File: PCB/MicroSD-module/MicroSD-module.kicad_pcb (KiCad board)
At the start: 2 copper layers, 24.4 x 41.9 mm, 16 parts, among them J1 Connector, K1 HYC77-TF09-200, U1 SE5218, U2 TXB0104PWR

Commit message: More OCD
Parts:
- moved C1 10.3 mm to (127.5, 111.9), turned to -90 degrees
- moved U1 8.39 mm to (130.0, 112.4)
- moved C2 8.13 mm to (132.7, 111.8)
- moved C3 4.46 mm to (124.7, 117.8)
- renumbered C3 to C2, C2 to C3
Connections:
- K1 pad SHIELD: (no net) -> GND
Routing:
- net GND: track 4.53 -> 41.7 mm, vias 7 -> 0
- net 5V_burgerDisk: track 46.5 -> 30.2 mm
- net 3V3: track 25.4 -> 30.6 mm, vias 2 -> 0
- net CS: track 23.9 -> 25.6 mm
- net MOSI_L: track 12.3 -> 14.0 mm
- net MISO: track 27.5 -> 28.5 mm
- net CS_L: track 14.6 -> 15.5 mm
- net MISO_L: track 9.04 -> 9.73 mm
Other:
- board text added: "https://colino.net"
- board text added: "© Colin Leroy-Mira"

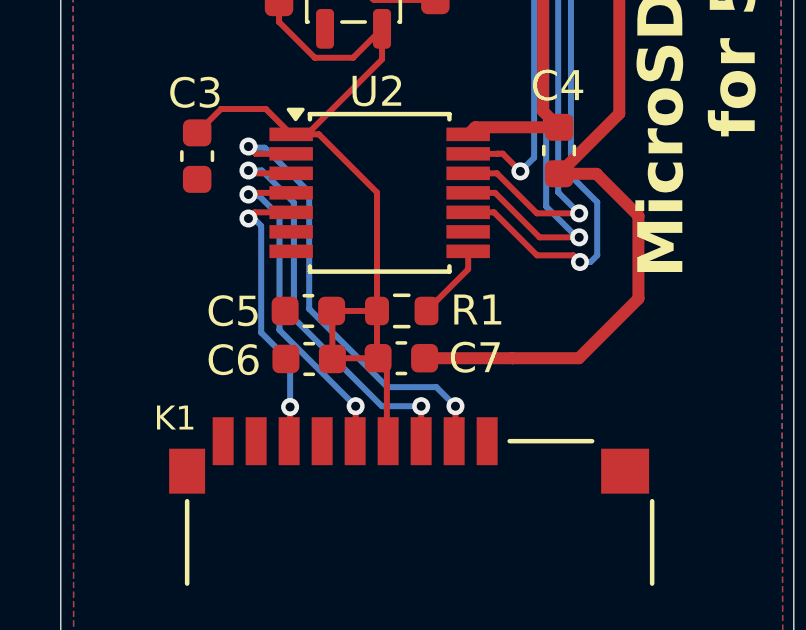
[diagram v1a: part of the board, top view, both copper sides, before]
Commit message: Fix microSD caps
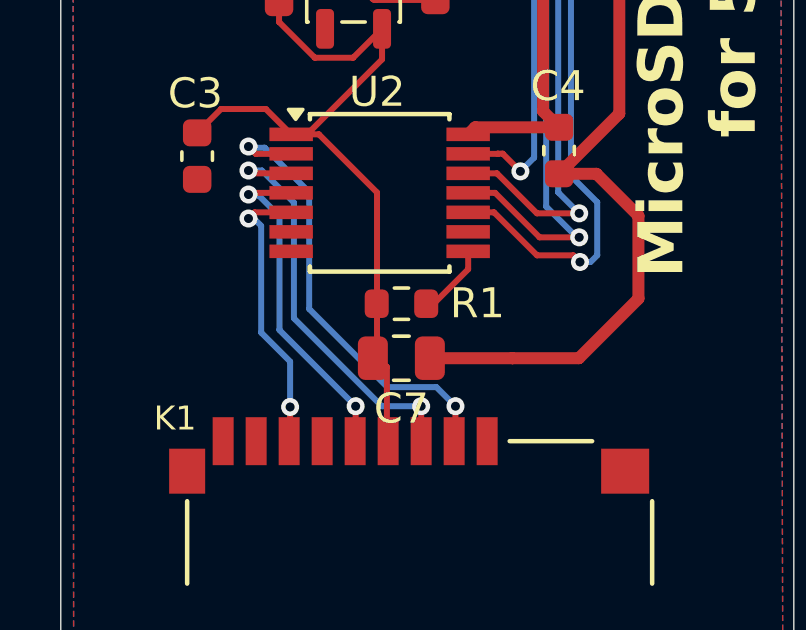
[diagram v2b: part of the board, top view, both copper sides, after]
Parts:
- removed C5: 100n, Capacitor_SMD:C_0603_1608Metric
- removed C6: 2u2, Capacitor_SMD:C_0603_1608Metric
- C7: value 100n -> 22uf; footprint Capacitor_SMD:C_0603_1608Metric -> Capacitor_SMD:C_0805_2012Metric
- moved R1 0.24 mm to (131.6, 122.7)
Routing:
- net 3V3: track 30.6 -> 26.0 mm

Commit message: OCD
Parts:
- moved C4 0.41 mm to (136.4, 117.6)
- renumbered C7 to C5
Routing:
- net 3V3: track 26.0 -> 27.8 mm
- net CS: track 25.6 -> 24.5 mm
- net GND: track 41.7 -> 42.4 mm
- net 5V_burgerDisk: track 30.2 -> 29.6 mm
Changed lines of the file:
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@@
 		(descr "Capacitor SMD 0805 (2012 Metric), square (rectangular) end terminal, IPC_7351 nominal, (Body size source: IPC-SM-782 page 76, https://www.pcb-3d.com/wordpress/wp-content/uploads/ipc-sm-782a_amendment_1_and_2.pdf, https://docs.google.com/spreadsheets/d/1BsfQQcO9C6DZCsRaXUlFlo91Tg2WpOkGARC1WS5S8t0/edit?usp=sharing), generated with kicad-footprint-generator")
 		(tags "capacitor")
-		(property "Reference" "C7"
-			(at 0 -1.68 180)
+		(property "Reference" "C5"
+			(at -2.7634 0.0362 180)
 			(layer "F.SilkS")
 			(effects
@@
 	(footprint "Capacitor_SMD:C_0603_1608Metric"
 		(layer "F.Cu")
-		(at 136.8044 117.6144 90)
+		(at 136.39 117.62 90)
 		(descr "Capacitor SMD 0603 (1608 Metric), square (rectangular) end terminal, IPC-7351 nominal, (Body size source: IPC-SM-782 page 76, https://www.pcb-3d.com/wordpress/wp-content/uploads/ipc-sm-782a_amendment_1_and_2.pdf), generated with kicad-footprint-generator")
 		(tags "capacitor")
@@
 	)
 	(segment
-		(start 138.0494 118.3894)
-		(end 136.8044 118.3894)
-		(width 0.4)
-		(layer "F.Cu")
-		(net 1)
-	)
-	(segment
-		(start 139.45 122.55)
-		(end 139.45 119.79)
+		(start 136.39 118.395)
+		(end 136.7988 118.395)
 		(width 0.4)
 		(layer "F.Cu")
@@
 	)
 	(segment
-		(start 136.8044 118.3894)
-		(end 138.811 116.3828)
+		(start 138.811 116.3828)
+		(end 138.811 100.3046)
 		(width 0.4)
 		(layer "F.Cu")
@@
 	)
 	(segment
-		(start 132.554 112.494)
-		(end 132.68 112.62)
+		(start 139.45 122.55)
+		(end 139.45 119.79)
 		(width 0.4)
 		(layer "F.Cu")
@@
 	)
 	(segment
-		(start 137.4638 124.5362)
-		(end 139.45 122.55)
+		(start 136.7988 118.395)
+		(end 138.811 116.3828)
 		(width 0.4)
 		(layer "F.Cu")
@@
 	)
 	(segment
-		(start 139.45 119.79)
-		(end 138.0494 118.3894)
+		(start 136.3956 118.3894)
+		(end 136.39 118.395)
 		(width 0.4)
 		(layer "F.Cu")
@@
 	)
 	(segment
-		(start 135.2462 124.5362)
-		(end 137.4638 124.5362)
+		(start 138.0494 118.3894)
+		(end 136.3956 118.3894)
 		(width 0.4)
 		(layer "F.Cu")
@@
 	)
 	(segment
-		(start 129.9525 111.2825)
-		(end 129.9525 111.944999)
+		(start 135.2462 124.5362)
+		(end 137.4638 124.5362)
 		(width 0.4)
 		(layer "F.Cu")
@@
 	)
 	(segment
-		(start 138.811 116.3828)
-		(end 138.811 100.3046)
+		(start 129.9525 111.2825)
+		(end 129.9525 111.944999)
 		(width 0.4)
 		(layer "F.Cu")
@@
 	)
 	(segment
+		(start 137.4638 124.5362)
+		(end 139.45 122.55)
+		(width 0.4)
+		(layer "F.Cu")
+		(net 1)
+	)
+	(segment
+		(start 139.45 119.79)
+		(end 138.0494 118.3894)
+		(width 0.4)
+		(layer "F.Cu")
+		(net 1)
+	)
+	(segment
 		(start 135.2462 124.5362)
 		(end 135.25 124.54)
@@
 	)
 	(segment
-		(start 135.514165 118.308035)
+		(start 134.93613 117.73)
 		(end 134.92413 117.718)
 		(width 0.2)
@@
 	)
 	(segment
-		(start 134.75567 117.7244)
-		(end 133.7734 117.7244)
+		(start 134.76207 117.718)
+		(end 134.75567 117.7244)
 		(width 0.2)
 		(layer "F.Cu")
@@
 	)
 	(segment
-		(start 134.76207 117.718)
-		(end 134.75567 117.7244)
+		(start 134.75567 117.7244)
+		(end 133.7734 117.7244)
+		(width 0.2)
+		(layer "F.Cu")
+		(net 2)
+	)
+	(segment
+		(start 135.1 117.73)
+		(end 134.93613 117.73)
 		(width 0.2)
 		(layer "F.Cu")
@@
 	)
 	(via
-		(at 135.514165 118.308035)
+		(at 135.1 117.73)
 		(size 0.6)
 		(drill 0.3)
@@
 	)
 	(segment
-		(start 135.9716 117.8506)
-		(end 135.9716 107.8716)
+		(start 135.9716 107.8716)
+		(end 130.17 102.07)
 		(width 0.2)
 		(layer "B.Cu")
@@
 	)
 	(segment
-		(start 135.9716 107.8716)
-		(end 130.17 102.07)
+		(start 135.1 117.73)
+		(end 135.9716 116.8584)
 		(width 0.2)
 		(layer "B.Cu")
@@
 	)
 	(segment
-		(start 130.17 102.07)
-		(end 127.8764 102.07)
+		(start 135.9716 116.8584)
+		(end 135.9716 107.8716)
 		(width 0.2)
 		(layer "B.Cu")
@@
 	)
 	(segment
-		(start 135.514165 118.308035)
-		(end 135.9716 117.8506)
+		(start 130.17 102.07)
+		(end 127.8764 102.07)
 		(width 0.2)
 		(layer "B.Cu")
@@
 	)
 	(segment
+		(start 136.39 116.845)
+		(end 136.3844 116.8394)
+		(width 0.4)
+		(layer "F.Cu")
+		(net 6)
+	)
+	(segment
+		(start 136.3844 116.8394)
+		(end 134.0084 116.8394)
+		(width 0.4)
+		(layer "F.Cu")
+		(net 6)
+	)
+	(segment
 		(start 132.68 111.07)
 		(end 134.23 111.07)
@@
 	)
 	(segment
+		(start 136.271 108.5)
+		(end 136.271 116.306)
+		(width 0.4)
+		(layer "F.Cu")
+		(net 6)
+	)
+	(segment
 		(start 130.9025 111.2825)
 		(end 132.4675 111.2825)
@@
 	)
 	(segment
-		(start 136.271 116.306)
-		(end 136.8044 116.8394)
+		(start 130.501499 110.219)
+		(end 130.9025 110.620001)
 		(width 0.4)
 		(layer "F.Cu")
@@
 	)
 	(segment
-		(start 130.501499 110.219)
-		(end 130.9025 110.620001)
+		(start 136.39 116.425)
+		(end 136.39 116.845)
 		(width 0.4)
 		(layer "F.Cu")
@@
 	)
 	(segment
-		(start 129.570112 110.219)
-		(end 130.501499 110.219)
+		(start 136.271 116.306)
+		(end 136.39 116.425)
 		(width 0.4)
 		(layer "F.Cu")
@@
 	)
 	(segment
-		(start 136.271 108.5)
-		(end 136.271 116.306)
+		(start 129.570112 110.219)
+		(end 130.501499 110.219)
 		(width 0.4)
 		(layer "F.Cu")
@@
 	)
 	(segment
-		(start 136.8044 116.8394)
-		(end 134.0084 116.8394)
-		(width 0.4)
+		(start 130.7348 119.0108)
+		(end 130.9025 118.8431)
+		(width 0.2)
 		(layer "F.Cu")
-		(net 6)
+		(net 7)
 	)
 	(segment
@@
 	)
 	(segment
-		(start 127.8734 117.0744)
-		(end 128.7984 117.0744)
-		(width 0.2)
-		(layer "F.Cu")
-		(net 7)
-	)
-	(segment
 		(start 130.7348 119.0108)
 		(end 130.7348 122.7102)
@@
 	)
 	(segment
-		(start 124.74 117.025)
-		(end 125.535 116.23)
+		(start 130.9025 118.8431)
+		(end 130.9025 113.5575)
 		(width 0.2)
 		(layer "F.Cu")
@@
 	)
 	(segment
-		(start 128.7984 117.0744)
-		(end 130.7348 119.0108)
+		(start 124.74 117.025)
+		(end 125.535 116.23)
 		(width 0.2)
 		(layer "F.Cu")

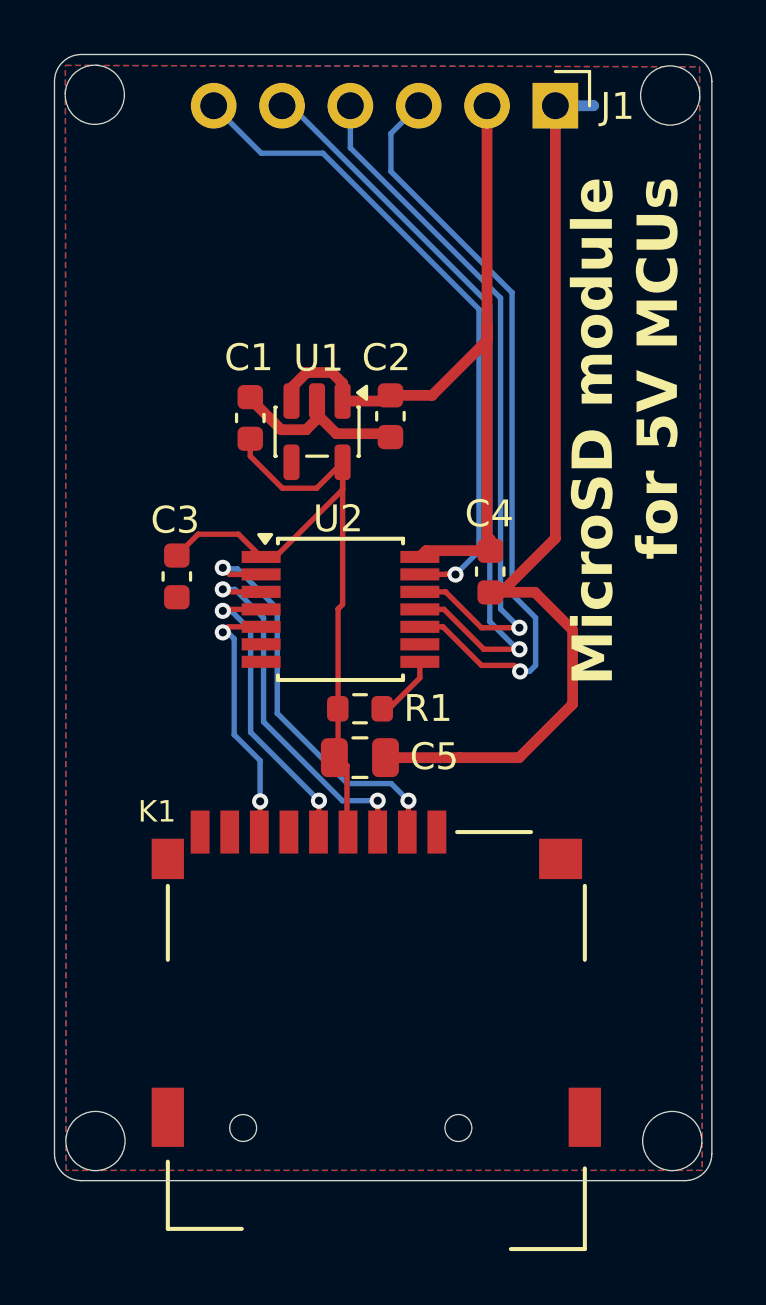
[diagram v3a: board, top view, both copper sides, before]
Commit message: fatter traces
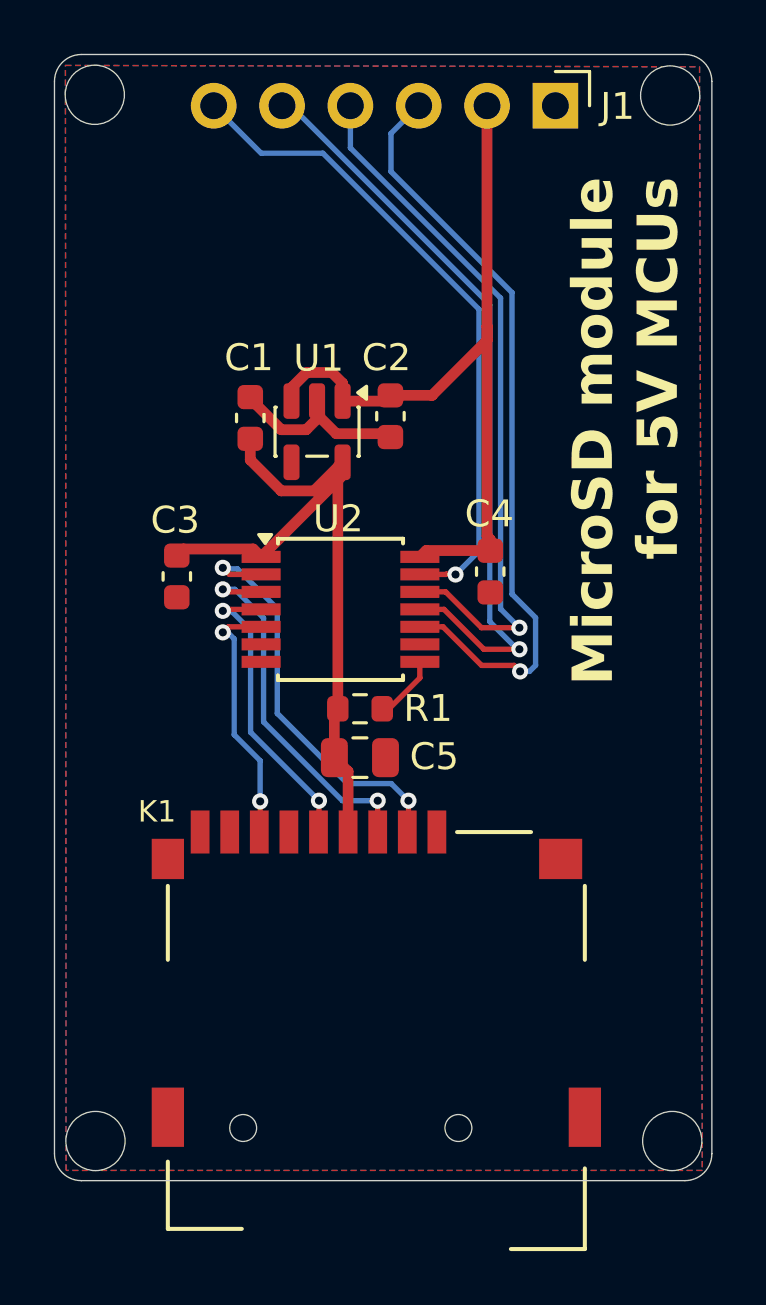
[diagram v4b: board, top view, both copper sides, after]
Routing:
- net GND: track 42.4 -> 7.24 mm
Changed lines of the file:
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@@
-	)
-	(segment
-		(start 136.39 118.395)
-		(end 136.7988 118.395)
-		(width 0.4)
-		(layer "F.Cu")
-		(net 1)
-	)
-	(segment
-		(start 132.3216 124.5362)
-		(end 135.2462 124.5362)
-		(width 0.4)
-		(layer "F.Cu")
-		(net 1)
-	)
-	(segment
-		(start 138.811 116.3828)
-		(end 138.811 100.3046)
-		(width 0.4)
-		(layer "F.Cu")
-		(net 1)
 	)
 	(segment
@@
 	)
 	(segment
-		(start 139.45 122.55)
-		(end 139.45 119.79)
-		(width 0.4)
-		(layer "F.Cu")
-		(net 1)
-	)
-	(segment
-		(start 136.7988 118.395)
-		(end 138.811 116.3828)
-		(width 0.4)
-		(layer "F.Cu")
-		(net 1)
-	)
-	(segment
-		(start 136.3956 118.3894)
-		(end 136.39 118.395)
-		(width 0.4)
-		(layer "F.Cu")
-		(net 1)
-	)
-	(segment
 		(start 129.9525 111.778388)
 		(end 130.668112 112.494)
@@
 	)
 	(segment
-		(start 138.0494 118.3894)
-		(end 136.3956 118.3894)
-		(width 0.4)
-		(layer "F.Cu")
-		(net 1)
-	)
-	(segment
-		(start 135.2462 124.5362)
-		(end 137.4638 124.5362)
-		(width 0.4)
-		(layer "F.Cu")
-		(net 1)
-	)
-	(segment
 		(start 129.9525 111.2825)
 		(end 129.9525 111.944999)
@@
 	)
 	(segment
-		(start 137.4638 124.5362)
-		(end 139.45 122.55)
-		(width 0.4)
-		(layer "F.Cu")
-		(net 1)
-	)
-	(segment
-		(start 139.45 119.79)
-		(end 138.0494 118.3894)
-		(width 0.4)
-		(layer "F.Cu")
-		(net 1)
-	)
-	(segment
-		(start 135.2462 124.5362)
-		(end 135.25 124.54)
-		(width 0.4)
-		(layer "F.Cu")
-		(net 1)
-	)
-	(segment
-		(start 138.811 100.3046)
-		(end 140.2254 100.3046)
-		(width 0.4)
-		(layer "B.Cu")
-		(net 1)
-	)
-	(segment
-		(start 140.2254 100.3046)
-		(end 140.23 100.3)
-		(width 0.4)
-		(layer "B.Cu")
-		(net 1)
-	)
-	(segment
 		(start 134.93613 117.73)
 		(end 134.92413 117.718)
@@
 	)
 	(segment
-		(start 130.7348 119.0108)
-		(end 130.9025 118.8431)
-		(width 0.2)
-		(layer "F.Cu")
-		(net 7)
-	)
-	(segment
-		(start 125.535 116.23)
-		(end 127.029 116.23)
-		(width 0.2)
-		(layer "F.Cu")
-		(net 7)
-	)
-	(segment
-		(start 127.47 113.329468)
-		(end 128.661532 114.521)
-		(width 0.2)
-		(layer "F.Cu")
-		(net 7)
-	)
-	(segment
-		(start 130.7348 124.4994)
-		(end 131.064 124.8286)
-		(width 0.2)
-		(layer "F.Cu")
-		(net 7)
-	)
-	(segment
-		(start 130.7348 119.0108)
-		(end 130.7348 122.7102)
-		(width 0.2)
-		(layer "F.Cu")
-		(net 7)
-	)
-	(segment
-		(start 131.064 124.8286)
-		(end 131.064 127.2596)
-		(width 0.2)
-		(layer "F.Cu")
-		(net 7)
-	)
-	(segment
-		(start 128.4056 117.0744)
+		(start 130.725 113.735)
+		(end 130.9025 113.5575)
+		(width 0.4)
+		(layer "F.Cu")
+		(net 7)
+	)
+	(segment
+		(start 127.47 113.470888)
+		(end 127.47 112.685)
+		(width 0.4)
+		(layer "F.Cu")
+		(net 7)
+	)
+	(segment
+		(start 127.578403 116.779403)
 		(end 127.8734 117.0744)
-		(width 0.2)
-		(layer "F.Cu")
-		(net 7)
-	)
-	(segment
-		(start 130.9025 114.5775)
-		(end 128.4056 117.0744)
-		(width 0.2)
-		(layer "F.Cu")
-		(net 7)
-	)
-	(segment
-		(start 129.939 114.521)
-		(end 130.9025 113.5575)
-		(width 0.2)
+		(width 0.4)
+		(layer "F.Cu")
+		(net 7)
+	)
+	(segment
+		(start 131.1062 125.0458)
+		(end 130.5966 124.5362)
+		(width 0.4)
+		(layer "F.Cu")
+		(net 7)
+	)
+	(segment
+		(start 130.5966 124.5362)
+		(end 130.5966 122.8484)
+		(width 0.4)
+		(layer "F.Cu")
+		(net 7)
+	)
+	(segment
+		(start 129.839 114.621)
+		(end 128.620112 114.621)
+		(width 0.4)
 		(layer "F.Cu")
 		(net 7)
@@
 	(segment
 		(start 130.9025 113.5575)
-		(end 130.9025 114.5775)
-		(width 0.2)
-		(layer "F.Cu")
-		(net 7)
-	)
-	(segment
-		(start 131.064 127.2596)
-		(end 131.1062 127.3018)
-		(width 0.2)
-		(layer "F.Cu")
-		(net 7)
-	)
-	(segment
-		(start 130.7348 122.7102)
+		(end 130.9025 114.0453)
+		(width 0.4)
+		(layer "F.Cu")
+		(net 7)
+	)
+	(segment
+		(start 124.985597 116.779403)
+		(end 127.578403 116.779403)
+		(width 0.4)
+		(layer "F.Cu")
+		(net 7)
+	)
+	(segment
+		(start 128.620112 114.621)
+		(end 127.47 113.470888)
+		(width 0.4)
+		(layer "F.Cu")
+		(net 7)
+	)
+	(segment
+		(start 130.9025 114.0453)
+		(end 127.8734 117.0744)
+		(width 0.4)
+		(layer "F.Cu")
+		(net 7)
+	)
+	(segment
+		(start 130.5966 122.8484)
 		(end 130.725 122.72)
-		(width 0.2)
+		(width 0.4)
+		(layer "F.Cu")
+		(net 7)
+	)
+	(segment
+		(start 131.1062 127.3018)
+		(end 131.1062 125.0458)
+		(width 0.4)
+		(layer "F.Cu")
+		(net 7)
+	)
+	(segment
+		(start 130.9025 113.5575)
+		(end 129.839 114.621)
+		(width 0.4)
+		(layer "F.Cu")
+		(net 7)
+	)
+	(segment
+		(start 124.74 117.025)
+		(end 124.985597 116.779403)
+		(width 0.4)
 		(layer "F.Cu")
 		(net 7)
@@
 	(segment
 		(start 130.725 122.72)
-		(end 130.7348 122.7298)
-		(width 0.2)
-		(layer "F.Cu")
-		(net 7)
-	)
-	(segment
-		(start 127.029 116.23)
-		(end 127.8734 117.0744)
-		(width 0.2)
-		(layer "F.Cu")
-		(net 7)
-	)
-	(segment
-		(start 130.7348 122.7298)
-		(end 130.7348 124.4994)
-		(width 0.2)
-		(layer "F.Cu")
-		(net 7)
-	)
-	(segment
-		(start 128.661532 114.521)
-		(end 129.939 114.521)
-		(width 0.2)
-		(layer "F.Cu")
-		(net 7)
-	)
-	(segment
-		(start 130.9025 118.8431)
-		(end 130.9025 113.5575)
-		(width 0.2)
-		(layer "F.Cu")
-		(net 7)
-	)
-	(segment
-		(start 124.74 117.025)
-		(end 125.535 116.23)
-		(width 0.2)
-		(layer "F.Cu")
-		(net 7)
-	)
-	(segment
-		(start 127.47 112.685)
-		(end 127.47 113.329468)
-		(width 0.2)
+		(end 130.725 113.735)
+		(width 0.4)
 		(layer "F.Cu")
 		(net 7)
@@
 		(layers "F.Cu" "B.Cu")
 		(hatch edge 0.5)
-		(connect_pads
+		(connect_pads yes
 			(clearance 0.5)
 		)
